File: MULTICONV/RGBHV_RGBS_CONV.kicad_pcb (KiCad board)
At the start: 2 copper layers, 100 x 100 mm, 111 parts, among them J1 DIGITAL RGB, J10 AUDIO1, J11 RGBHV_2, J12 AUDIO2, J15 RGBS_OUT1, J16 RGBS_OUT2, J17 VIN, J2 VGA DB15, J3 ANALOG RGB DA15, J4 X1, J5 DIGITAL_RGBHV_1, J6 ANALOG RGB, J7 DIGITAL_RGBHV_2, J8 SWITCHER, J9 RGBHV_1, U1 OUT_GND_IN_3.3V, U2 74HC86, U3 OUT_IN_GND_3.3V, U4 IN_OUT_GND_3.3V

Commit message: Rev1.5 リリース候補
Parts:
- removed J1: DIGITAL RGB, ryuk_lib:DIN 8 PCB
- removed J4: X1, ryuk_lib:DIN_6_PCB
- removed J5: DIGITAL_RGBHV_1, Connector_JST:JST_XH_B8B-XH-A_1x08_P2.50mm_Vertical
- removed J7: DIGITAL_RGBHV_2, Connector_JST:JST_XH_B8B-XH-A_1x08_P2.50mm_Vertical
- removed PIN01 (x2), PIN02 (x2), PIN03 (x2), PIN04 (x2), PIN05 (x2), PIN06 (x2), PIN07 (x2), PIN08 (x2), PIN09 (x2), PIN10 (x2), PIN11 (x2), PIN12 (x2), PIN13 (x2), PIN14 (x2), PIN15 (x2), PIN16 (x2), PIN17 (x2), PIN18 (x2), PIN19 (x2), PIN20 (x2), PIN21 (x2), PIN22 (x2), PIN23 (x2), PIN24 (x2), PIN25 (x2), PIN26 (x2), PIN27 (x2), PIN28 (x2), PIN29 (x2), PIN30 (x2), PIN31 (x2), PIN32 (x2), PIN33 (x2), PIN34 (x2), PIN35 (x2), PIN36 (x2): Pin_2.54, ryuk_lib:Pin_2.54
- added C10: 0.1uF, Capacitor_SMD:C_0603_1608Metric, F.Cu at (95.9, 137.2)
- added C11: 0.1uF, Capacitor_SMD:C_0603_1608Metric, F.Cu at (100.8, 121.0)
- added C12: 0.1uF, Capacitor_SMD:C_0603_1608Metric, F.Cu at (102.6, 103.9)
- added C13: 0.1uF, Capacitor_SMD:C_0603_1608Metric, F.Cu at (94.5, 121.0)
- added C2: 510pF, Capacitor_THT:C_Disc_D5.0mm_W2.5mm_P5.00mm, F.Cu at (102.3, 139.6)
- added C7: 0.1uF, Capacitor_THT:C_Disc_D5.0mm_W2.5mm_P5.00mm, F.Cu at (94.5, 118.5)
- added C8: 10uF, Capacitor_SMD:C_1206_3216Metric, F.Cu at (117.7, 86.3)
- added C9: 10uF, Capacitor_SMD:C_1206_3216Metric, F.Cu at (117.2, 104.9)
- added H10: M4, MountingHole:MountingHole_4.3mm_M4, F.Cu at (55.0, 122.0)
- added H11: M4, MountingHole:MountingHole_4.3mm_M4, F.Cu at (145.0, 102.0)
- added H12: M4, MountingHole:MountingHole_4.3mm_M4, F.Cu at (145.0, 122.0)
- added H13: M4, MountingHole:MountingHole_4.3mm_M4, F.Cu at (55.0, 96.2)
- added H14: M4, MountingHole:MountingHole_4.3mm_M4, F.Cu at (145.0, 96.0)
- added H5: M3, MountingHole:MountingHole_3.2mm_M3, F.Cu at (135.0, 102.0)
- added H6: M3, MountingHole:MountingHole_3.2mm_M3, F.Cu at (65.0, 102.0)
- added H7: M3, MountingHole:MountingHole_3.2mm_M3, F.Cu at (135.0, 122.0)
- added H8: M3, MountingHole:MountingHole_3.2mm_M3, F.Cu at (65.0, 122.0)
- added H9: M4, MountingHole:MountingHole_4.3mm_M4, F.Cu at (55.0, 102.0)
- added J13: SE`PARATE RGBHV OUT, Connector_JST:JST_XH_B8B-XH-A_1x08_P2.50mm_Vertical, F.Cu at (87.6, 137.1)
- added R12: 620R, Resistor_THT:R_Axial_DIN0207_L6.3mm_D2.5mm_P10.16mm_Horizontal, F.Cu at (99.1, 144.8)
- added R13: 681KR, Resistor_THT:R_Axial_DIN0207_L6.3mm_D2.5mm_P10.16mm_Horizontal, F.Cu at (97.6, 123.5)
- added R14: 470R, Resistor_THT:R_Axial_DIN0207_L6.3mm_D2.5mm_P10.16mm_Horizontal, F.Cu at (92.8, 144.8)
- added R15: 150R, Resistor_SMD:R_0603_1608Metric, F.Cu at (109.0, 99.9)
- added REF**: OSHW-Logo2_9.8x8mm_SilkScreen, Symbol:OSHW-Logo2_9.8x8mm_SilkScreen, B.Cu at (135.0, 81.0)
- added REF**: OSHW-Logo2_9.8x8mm_SilkScreen, Symbol:OSHW-Logo2_9.8x8mm_SilkScreen, F.Cu at (135.0, 81.0)
- added SW1: HSYNC/CSYNC, ryuk_lib:2MS1T1B4M7QES, F.Cu at (76.8, 157.6)
- added SW2: STRIPPER, ryuk_lib:2MS1T1B4M7QES, F.Cu at (69.9, 157.6)
- added SW3: BYPASS HC86, ryuk_lib:2MS1T1B4M7QES, F.Cu at (63.3, 157.6)
- H1, H2, H3, H4: footprint MountingHole:MountingHole_4.3mm_M4_Pad -> MountingHole:MountingHole_4.3mm_M4
- R1, R2: footprint Resistor_THT:R_Axial_DIN0207_L6.3mm_D2.5mm_P10.16mm_Horizontal -> Resistor_SMD:R_0603_1608Metric
- R3: value 150R -> 10KR; footprint Resistor_THT:R_Axial_DIN0207_L6.3mm_D2.5mm_P10.16mm_Horizontal -> Resistor_SMD:R_0603_1608Metric
- U1: value OUT_GND_IN_3.3V -> 3V3_REG; footprint Package_TO_SOT_THT:TO-220-3_Vertical -> ryuk_lib:PIN_Unified_LDO
- U3: value OUT_IN_GND_3.3V -> EL1883; footprint Package_TO_SOT_THT:TO-220-3_Vertical -> Package_SO:SOIC-8_3.9x4.9mm_P1.27mm
- U4: value IN_OUT_GND_3.3V -> NL7SZ57; footprint Package_TO_SOT_THT:TO-220-3_Vertical -> Package_SO:TSOP-6_1.65x3.05mm_P0.95mm
- moved C4 69.8 mm to (95.9, 139.7), turned to 90 degrees
- moved J12 69.1 mm to (90.4, 161.8)
- moved U3 56.8 mm to (97.7, 128.9), turned to 90 degrees
- moved U4 50.6 mm to (98.0, 108.0), turned to 0 degrees
- moved C6 46.3 mm to (100.8, 123.5), turned to 90 degrees
- moved R2 41.6 mm to (121.9, 127.6)
- moved R3 32.4 mm to (105.8, 99.9)
- moved R1 29.6 mm to (112.0, 127.3), turned to 270 degrees
- moved C5 19.9 mm to (121.1, 105.0), turned to 0 degrees
- moved C3 16.8 mm to (121.6, 86.2)
- moved R10 12.5 mm to (112.2, 106.4)
- moved R11 12.5 mm to (102.2, 87.5)
- moved U1 12.0 mm to (121.2, 95.6), turned to 90 degrees
- moved R9 10.8 mm to (109.0, 106.4)
- moved J11 10.2 mm to (94.1, 101.6)
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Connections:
- C4 pad 1: Net-(C3-Pad1) -> Net-(C10-Pad1)
- C4 pad 2: GND -> Net-(C10-Pad2)
- C6 pad 1: +3V3 -> Net-(C11-Pad1)
- J15 pad 5: Net-(J15-Pad5) -> (no net)
- J15 pad 6: Net-(J15-Pad6) -> VSYNC
- J15 pad 7: Net-(J15-Pad7) -> (no net)
- J16 pad 5: Net-(J16-Pad5) -> (no net)
- J16 pad 6: Net-(J16-Pad6) -> VSYNC
- J16 pad 7: Net-(J16-Pad7) -> (no net)
- J2 pad 12: Net-(J2-Pad12) -> (no net)
- J2 pad 15: Net-(J2-Pad15) -> (no net)
- J2 pad 4: Net-(J2-Pad4) -> (no net)
- J2 pad 5: Net-(J2-Pad5) -> (no net)
- J2 pad 9: Net-(J2-Pad9) -> (no net)
- J3 pad 13: Net-(J3-Pad13) -> (no net)
- J3 pad 14: HSYNC -> Net-(J3-Pad14)
- J3 pad 7: Net-(J3-Pad7) -> (no net)
- J6 pad 10: Net-(J6-Pad10) -> (no net)
- J6 pad 13: Net-(J6-Pad13) -> (no net)
- J6 pad 16: Net-(J6-Pad16) -> (no net)
- J6 pad 2: Net-(J6-Pad2) -> (no net)
- R1 pad 1: DIGITAL_R -> Net-(R1-Pad1)
- R1 pad 2: R -> VSYNC
- R10 pad 2: CSYNC -> Net-(R10-Pad2)
- R2 pad 1: DIGITAL_G -> HSYNC
- R2 pad 2: G -> Net-(R2-Pad2)
- R3 pad 1: DIGITAL_B -> Net-(R3-Pad1)
- R3 pad 2: B -> +3V3
- R4 pad 2: Net-(R4-Pad2) -> Net-(R1-Pad1)
- R5 pad 2: Net-(R4-Pad2) -> Net-(R1-Pad1)
- R6 pad 2: Net-(R6-Pad2) -> Net-(R2-Pad2)
- R7 pad 2: Net-(R6-Pad2) -> Net-(R2-Pad2)
- R8 pad 1: Net-(R8-Pad1) -> Net-(R3-Pad1)
- R9 pad 2: CSYNC -> Net-(R10-Pad2)
- U2 pad 1: Net-(R4-Pad2) -> Net-(R1-Pad1)
- U2 pad 13: Net-(R8-Pad1) -> Net-(R3-Pad1)
- U2 pad 2: Net-(R6-Pad2) -> Net-(R2-Pad2)
- U2 pad 6: Net-(U2-Pad6) -> (no net)
- U2 pad 8: Net-(U2-Pad8) -> (no net)
- U3 pad 1: GND -> Net-(R14-Pad2)
- U3 pad 2: Net-(C3-Pad1) -> Net-(C10-Pad2)
- U3 pad 3: +3V3 -> Net-(J13-Pad5)
- U4 pad 1: GND -> Net-(R1-Pad1)
- U4 pad 2: +3V3 -> GND
- U4 pad 3: Net-(C3-Pad1) -> Net-(R1-Pad1)
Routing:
- net Net-(R10-Pad2): track 0.00 -> 115.7 mm
- net CSYNC: track 31.3 -> 115.9 mm
- net Net-(J3-Pad9): track 0.00 -> 53.5 mm
- net DIGITAL_R: track 50.6 -> 0.00 mm
- net DIGITAL_B: track 49.2 -> 0.00 mm
- net DIGITAL_G: track 44.6 -> 0.00 mm
- net Net-(J3-Pad14): track 0.00 -> 43.9 mm
- net Net-(R2-Pad2): track 0.00 -> 38.0 mm, vias 0 -> 1
- net VSYNC: track 210.5 -> 176.0 mm
- net Net-(R10-Pad1): track 10.0 -> 44.1 mm
- net Net-(R1-Pad1): track 0.00 -> 31.1 mm, vias 0 -> 1
- net GND: track 44.4 -> 13.4 mm, vias 0 -> 1
- net Net-(J13-Pad5): track 0.00 -> 31.0 mm
- net AUDIO_L: track 179.6 -> 148.6 mm, vias 0 -> 1
- net R: track 212.5 -> 182.8 mm
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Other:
- board text added: "A_L"
- board text added: "A_R"
- board text added: "B"
- board text added: "G"
- board text added: "H"
- board text added: "IDC EXTRA DA15 CONNECTOR"
- board text added: "ISL59885 Configuration R13 - do not use C6 - 0.056uF"
- board text added: "Maybe can use 74HC86 74AC86 74AHC86"
- board text added: "R"
- board text added: "RGB MULTI CONVERTER REV 1.5 SEP/2022 C) @antarcticlion Licensed under CERN-OHL-W v2"
- board text added: "S"
- board text added: "SYNC SEPARATER OUTPUT"
- board text added: "V"
- board text added: "maybe can use 74LVC1G57 NL7SZ57"
- board text removed: "1117"
- board text removed: "48033"
- board text removed: "7533-1"
- board text removed: "RGB MULTI CONVERTER REV 1.0D JUL/2021 (C) @antarcticlion"

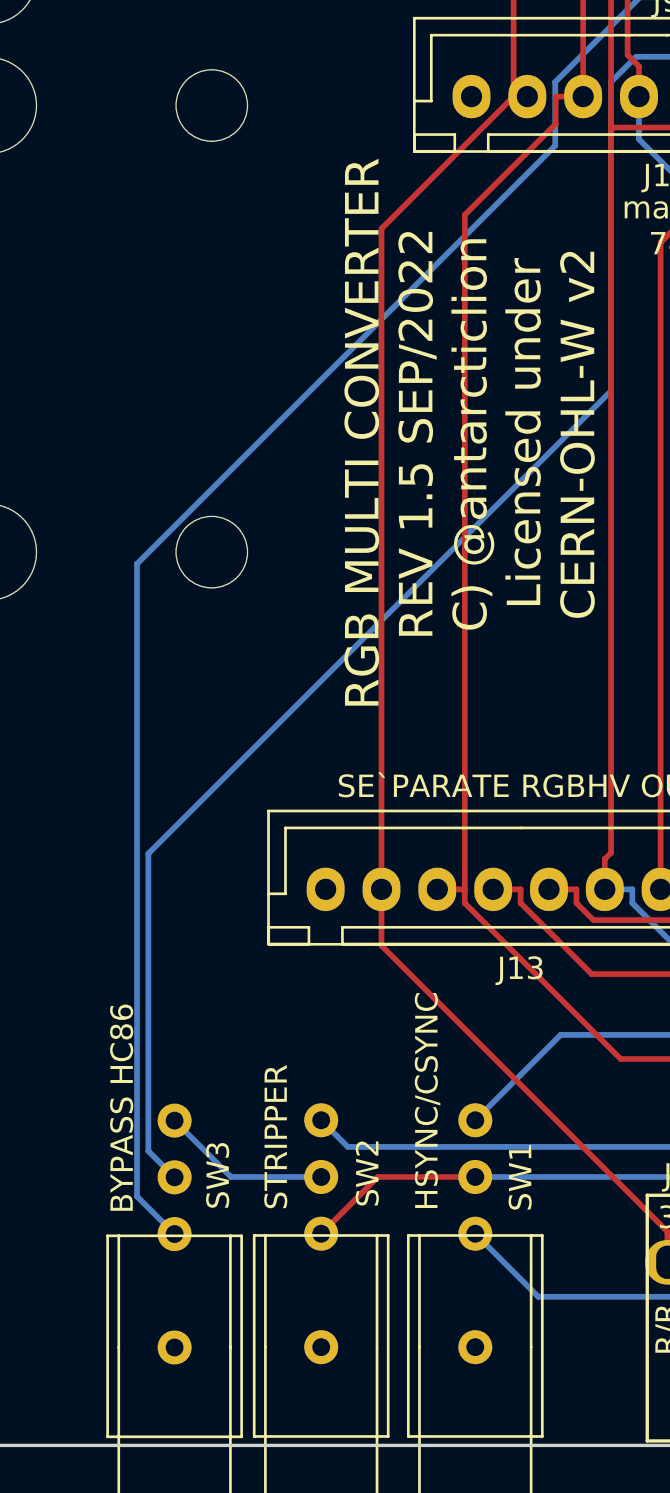
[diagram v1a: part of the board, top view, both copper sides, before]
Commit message: Fix switch hole size
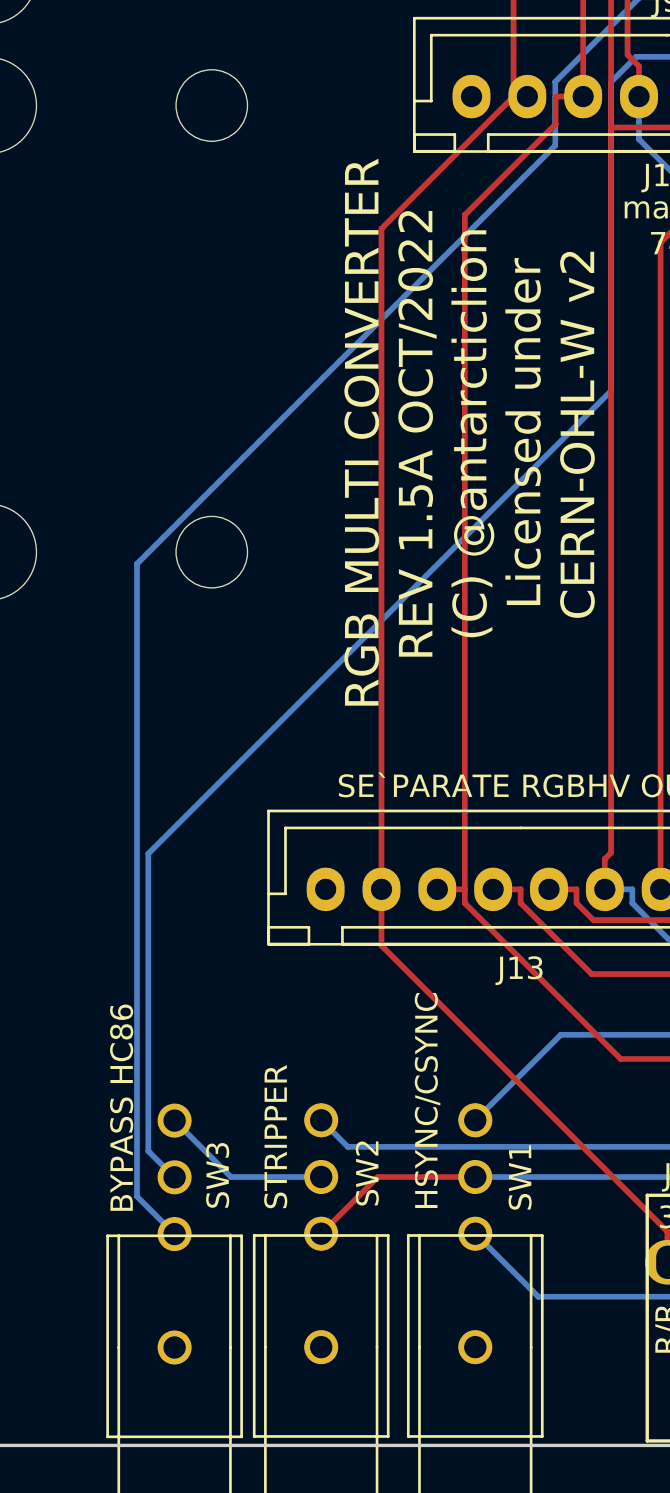
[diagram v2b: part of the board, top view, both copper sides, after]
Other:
- board text added: "RGB MULTI CONVERTER REV 1.5A OCT/2022 (C) @antarcticlion Licensed under CERN-OHL-W v2"
- board text removed: "RGB MULTI CONVERTER REV 1.5 SEP/2022 C) @antarcticlion Licensed under CERN-OHL-W v2"
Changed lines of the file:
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@@
     (mod_text_size 1 1)
     (mod_text_width 0.15)
-    (pad_size 4.3 8)
-    (pad_drill 4.3)
+    (pad_size 1.524 1.524)
+    (pad_drill 1)
     (pad_to_mask_clearance 0.2)
     (solder_mask_min_width 0.25)
@@
     (fp_line (start 3 -4) (end 3 5) (layer F.SilkS) (width 0.12))
     (fp_line (start 3 5) (end 2.5 5) (layer F.SilkS) (width 0.12))
-    (pad 0 thru_hole circle (at 0 0 180) (size 1.524 1.524) (drill 0.8) (layers *.Cu *.Mask))
-    (pad 3 thru_hole circle (at 0 10.16 180) (size 1.524 1.524) (drill 0.8) (layers *.Cu *.Mask)
+    (pad 0 thru_hole circle (at 0 0 180) (size 1.524 1.524) (drill 1) (layers *.Cu *.Mask))
+    (pad 3 thru_hole circle (at 0 10.16 180) (size 1.524 1.524) (drill 1) (layers *.Cu *.Mask)
       (net 21 "Net-(SW2-Pad2)"))
-    (pad 2 thru_hole circle (at 0 7.62 180) (size 1.524 1.524) (drill 0.8) (layers *.Cu *.Mask)
+    (pad 2 thru_hole circle (at 0 7.62 180) (size 1.524 1.524) (drill 1) (layers *.Cu *.Mask)
       (net 7 CSYNC))
-    (pad 1 thru_hole circle (at 0 5.08 180) (size 1.524 1.524) (drill 0.8) (layers *.Cu *.Mask)
+    (pad 1 thru_hole circle (at 0 5.08 180) (size 1.524 1.524) (drill 1) (layers *.Cu *.Mask)
       (net 18 "Net-(R10-Pad2)"))
   )
@@
     (fp_line (start 3 -4) (end 3 5) (layer F.SilkS) (width 0.12))
     (fp_line (start 3 5) (end 2.5 5) (layer F.SilkS) (width 0.12))
-    (pad 0 thru_hole circle (at 0 0 180) (size 1.524 1.524) (drill 0.8) (layers *.Cu *.Mask))
-    (pad 3 thru_hole circle (at 0 10.16 180) (size 1.524 1.524) (drill 0.8) (layers *.Cu *.Mask)
+    (pad 0 thru_hole circle (at 0 0 180) (size 1.524 1.524) (drill 1) (layers *.Cu *.Mask))
+    (pad 3 thru_hole circle (at 0 10.16 180) (size 1.524 1.524) (drill 1) (layers *.Cu *.Mask)
       (net 20 "Net-(R14-Pad1)"))
-    (pad 2 thru_hole circle (at 0 7.62 180) (size 1.524 1.524) (drill 0.8) (layers *.Cu *.Mask)
+    (pad 2 thru_hole circle (at 0 7.62 180) (size 1.524 1.524) (drill 1) (layers *.Cu *.Mask)
       (net 21 "Net-(SW2-Pad2)"))
-    (pad 1 thru_hole circle (at 0 5.08 180) (size 1.524 1.524) (drill 0.8) (layers *.Cu *.Mask)
+    (pad 1 thru_hole circle (at 0 5.08 180) (size 1.524 1.524) (drill 1) (layers *.Cu *.Mask)
       (net 3 HSYNC))
   )
@@
     (fp_line (start 3 -4) (end 3 5) (layer F.SilkS) (width 0.12))
     (fp_line (start 3 5) (end 2.5 5) (layer F.SilkS) (width 0.12))
-    (pad 0 thru_hole circle (at 0 0 180) (size 1.524 1.524) (drill 0.8) (layers *.Cu *.Mask))
-    (pad 3 thru_hole circle (at 0 10.16 180) (size 1.524 1.524) (drill 0.8) (layers *.Cu *.Mask)
+    (pad 0 thru_hole circle (at 0 0 180) (size 1.524 1.524) (drill 1) (layers *.Cu *.Mask))
+    (pad 3 thru_hole circle (at 0 10.16 180) (size 1.524 1.524) (drill 1) (layers *.Cu *.Mask)
       (net 15 "Net-(J3-Pad14)"))
-    (pad 2 thru_hole circle (at 0 7.62 180) (size 1.524 1.524) (drill 0.8) (layers *.Cu *.Mask)
+    (pad 2 thru_hole circle (at 0 7.62 180) (size 1.524 1.524) (drill 1) (layers *.Cu *.Mask)
       (net 3 HSYNC))
-    (pad 1 thru_hole circle (at 0 5.08 180) (size 1.524 1.524) (drill 0.8) (layers *.Cu *.Mask)
+    (pad 1 thru_hole circle (at 0 5.08 180) (size 1.524 1.524) (drill 1) (layers *.Cu *.Mask)
       (net 13 "Net-(J3-Pad9)"))
   )
@@
     (effects (font (size 1.5 1.5) (thickness 0.3)) (justify mirror))
   )
-  (gr_text "RGB MULTI CONVERTER\nREV 1.5 SEP/2022 \nC) @antarcticlion\nLicensed under\nCERN-OHL-W v2" (at 76.5 116.8 90) (layer B.SilkS)
+  (gr_text "RGB MULTI CONVERTER\nREV 1.5A OCT/2022 \n(C) @antarcticlion\nLicensed under\nCERN-OHL-W v2" (at 76.5 116.8 90) (layer B.SilkS)
     (effects (font (size 1.5 1.5) (thickness 0.3)) (justify mirror))
   )
-  (gr_text "RGB MULTI CONVERTER\nREV 1.5 SEP/2022 \nC) @antarcticlion\nLicensed under\nCERN-OHL-W v2" (at 76.6 116.7 90) (layer F.SilkS)
+  (gr_text "RGB MULTI CONVERTER\nREV 1.5A OCT/2022 \n(C) @antarcticlion\nLicensed under\nCERN-OHL-W v2" (at 76.6 116.7 90) (layer F.SilkS)
     (effects (font (size 1.5 1.5) (thickness 0.3)))
   )
